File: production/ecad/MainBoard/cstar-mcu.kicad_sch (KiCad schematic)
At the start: 58 parts, among them J1 USB_C_Receptacle_USB2.0, J2 USB_C_Receptacle_USB2.0, J3 RX connect, J4 TX connect, J5 Ultra_1, J6 Ultra_2, J7 Ultra_3, J8 Ultra_4, Q1 AO3400A, Q2 AO3400A, Q3 AO3400A, Q4 AO3400A, SW1 SW_Push, SW2 SW_Push, SW3 SW_Push, SW4 SW_Push, U1 ESP32-WROOM-32UE_M113EH6400UH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, U2 CP2102N-A01-GQFN28, U3 TXB0104DR, U4 CP2102N-A01-GQFN28, U5 TXB0104DR, U6 ESP32-WROOM-32UE_M113EH6400UH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

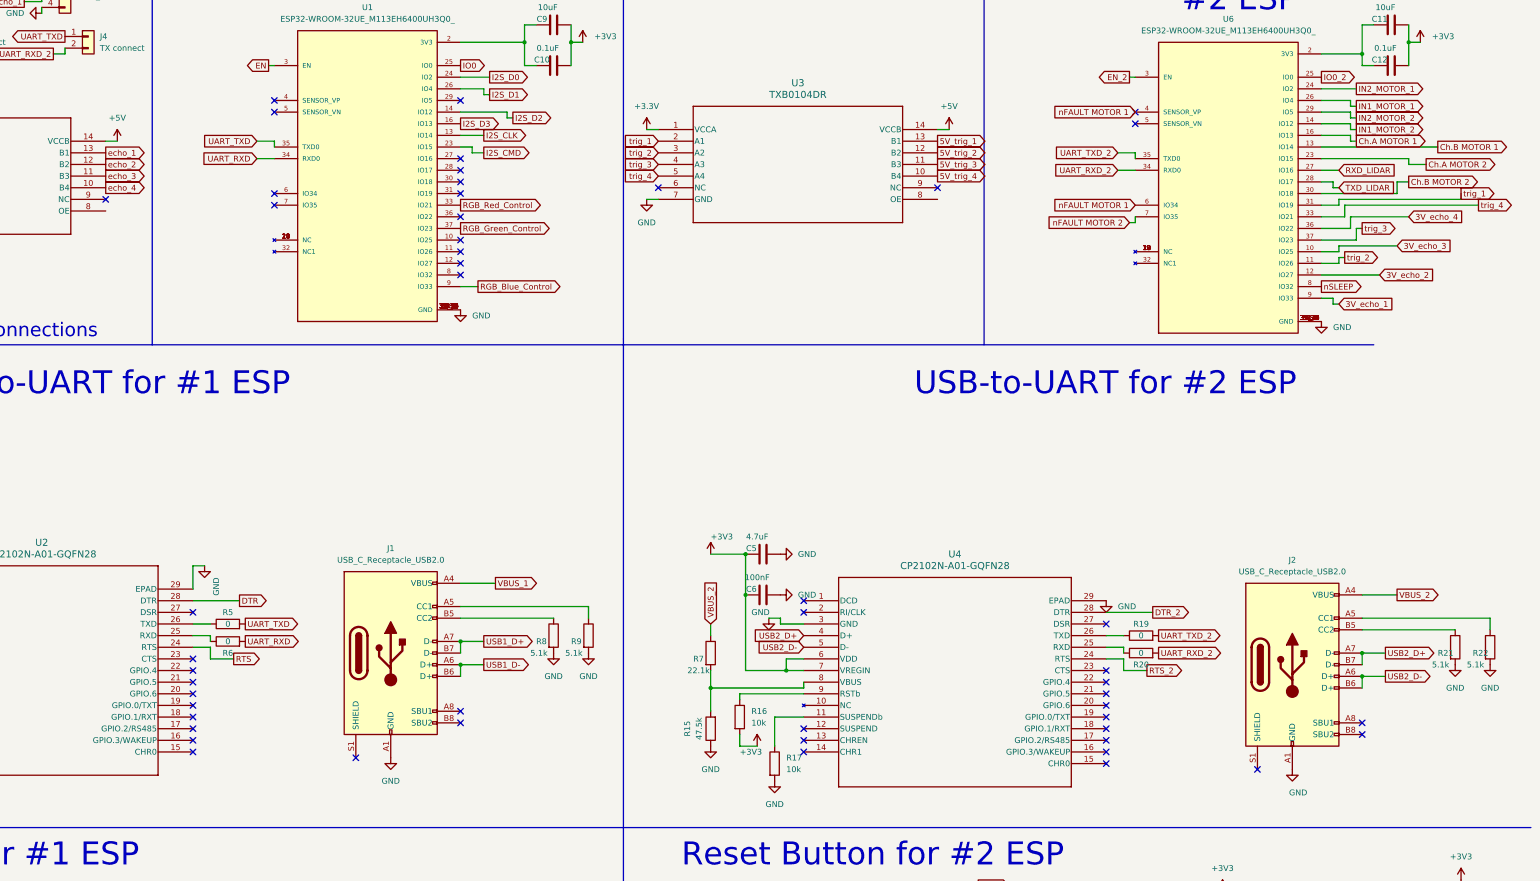
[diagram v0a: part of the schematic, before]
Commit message: Reversion of overcommited files
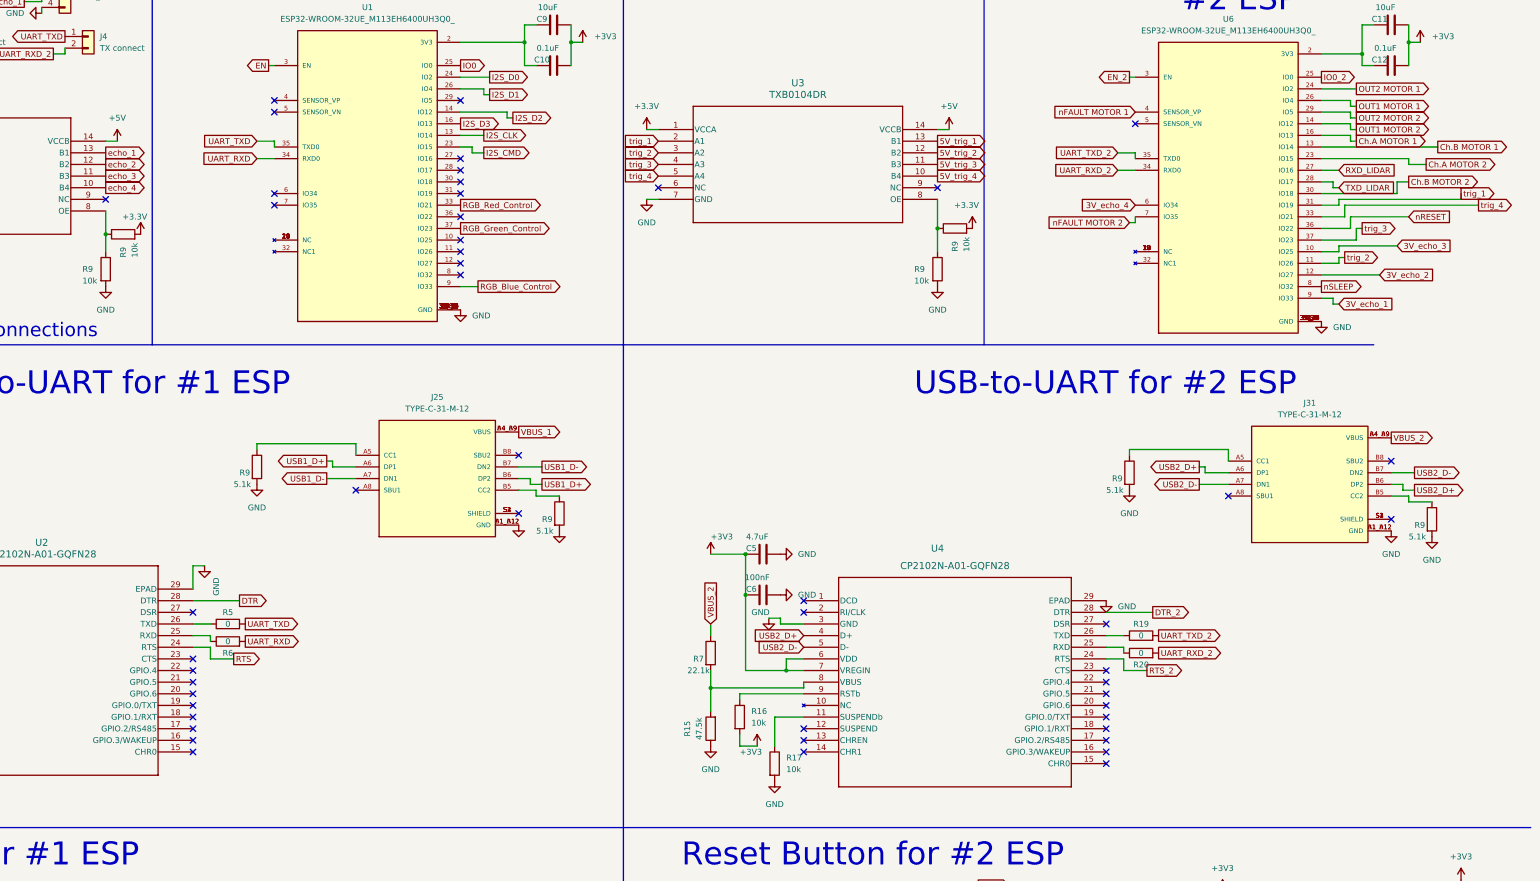
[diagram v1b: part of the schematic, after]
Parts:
- removed J1, J2: USB_C_Receptacle_USB2.0, CSTAR-MainBoard-Footprints:USBCONN-GCT_USB4105GFA, symbol Connector:USB_C_Receptacle_USB2.0
- removed R21, R22, R8, R9: 5.1k, Resistor_SMD:R_0805_2012Metric, symbol Device:R
- added J25, J31: TYPE-C-31-M-12, CSTAR-MainBoard-Footprints:HRO_TYPE-C-31-M-12, symbol TYPE-C-31-M-12:TYPE-C-31-M-12
- added R9 (x4): 10k, Resistor_SMD:R_0805_2012Metric, symbol Device:R
- added R9 (x4): 5.1k, Resistor_SMD:R_0805_2012Metric, symbol Device:R
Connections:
- net +3.3V: now also R9.2, R9.2
- net 3V_echo_4: now also U6.6 (IO34); no longer U6.36 (IO22)
- net GND: now also J25.A1_B12 (GND), J25.B1_A12 (GND), J31.A1_B12 (GND), J31.B1_A12 (GND), R9.2, R9.2, R9.2, R9.2, R9.2, R9.2
- net USB1_D+: now also J25.A6 (DP1), J25.B6 (DP2)
- net USB1_D-: now also J25.A7 (DN1), J25.B7 (DN2)
- net USB2_D+: now also J31.A6 (DP1), J31.B6 (DP2)
- net USB2_D-: now also J31.A7 (DN1), J31.B7 (DN2)
- net VBUS_1: now also J25.A4_B9 (VBUS), J25.B4_A9 (VBUS)
- net VBUS_2: now also J31.A4_B9 (VBUS), J31.B4_A9 (VBUS)
- net nFAULT MOTOR 1: no longer U6.6 (IO34)
- net at U5.8 (OE): now also R9.1, R9.1
- net at U3.8 (OE): now also R9.1, R9.1
- net IN1_MOTOR_1 renamed OUT1 MOTOR 1
- net IN1_MOTOR_2 renamed OUT1 MOTOR 2
- net IN2_MOTOR_1 renamed OUT2 MOTOR 1
- net IN2_MOTOR_2 renamed OUT2 MOTOR 2
- new net: J31.B5 (CC2), R9.1
- new net: J25.A5 (CC1), R9.1
- new net: J31.A5 (CC1), R9.1
- new net: J31.S1 (SHIELD), J31.S2 (SHIELD), J31.S3 (SHIELD), J31.S4 (SHIELD)
- new net: J25.B5 (CC2), R9.1
- new net: J25.S1 (SHIELD), J25.S2 (SHIELD), J25.S3 (SHIELD), J25.S4 (SHIELD)
- new net nRESET: U6.36 (IO22)
- no-connect marks 56 -> 55

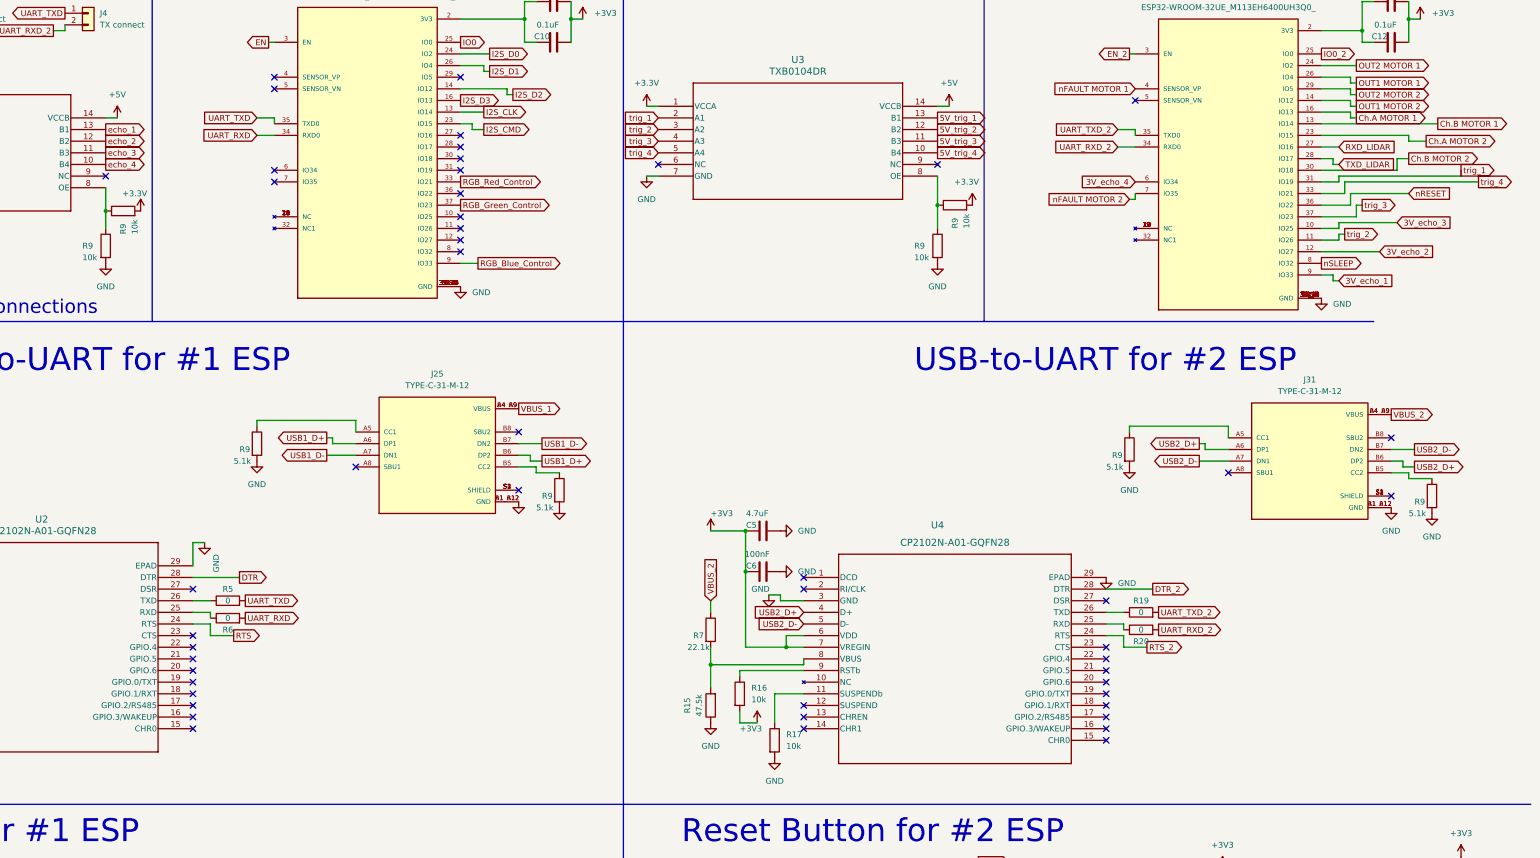
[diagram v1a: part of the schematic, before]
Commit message: "Added Backup Connector"
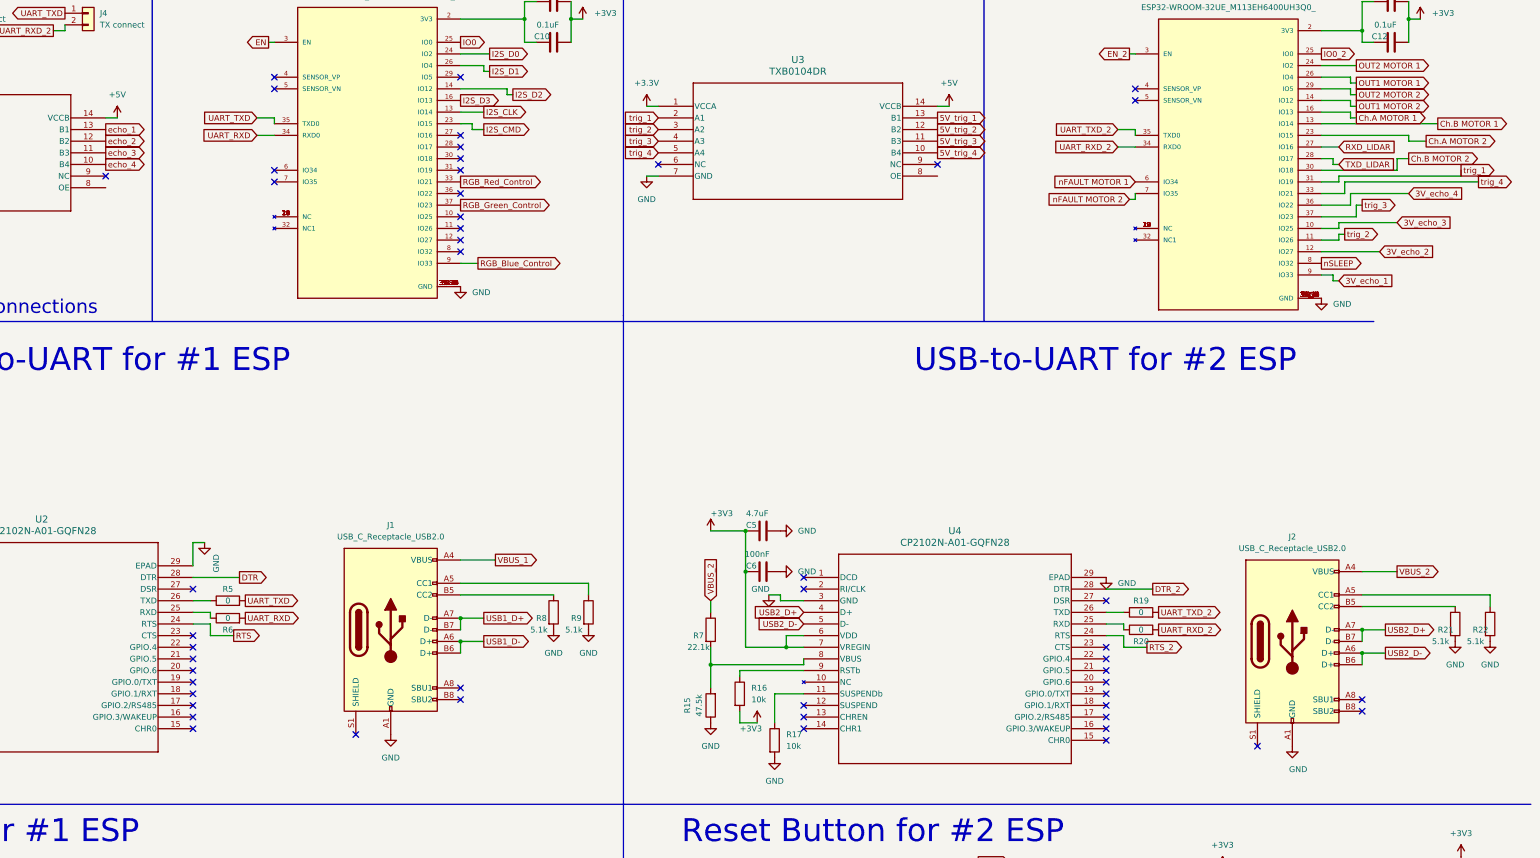
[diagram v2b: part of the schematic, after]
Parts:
- removed J25, J31: TYPE-C-31-M-12, CSTAR-MainBoard-Footprints:HRO_TYPE-C-31-M-12, symbol TYPE-C-31-M-12:TYPE-C-31-M-12
- removed R9 (x4): 10k, Resistor_SMD:R_0805_2012Metric, symbol Device:R
- removed R9 (x4): 5.1k, Resistor_SMD:R_0805_2012Metric, symbol Device:R
- added J1, J2: USB_C_Receptacle_USB2.0, CSTAR-MainBoard-Footprints:USBCONN-GCT_USB4105GFA, symbol Connector:USB_C_Receptacle_USB2.0
- added R21, R22, R8, R9: 5.1k, Resistor_SMD:R_0805_2012Metric, symbol Device:R
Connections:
- net nRESET is gone; now on net 3V_echo_4: U6.36 (IO22)
- net 3V_echo_4: no longer U6.6 (IO34)
- net GND: now also J1.A1 (GND), J1.A12 (GND), J1.B1 (GND), J1.B12 (GND), J2.A1 (GND), J2.A12 (GND), J2.B1 (GND), J2.B12 (GND), R21.2, R22.2, R8.2, R9.2
- net USB1_D+: now also J1.A7 (D-), J1.B7 (D-)
- net USB1_D-: now also J1.A6 (D+), J1.B6 (D+)
- net USB2_D+: now also J2.A7 (D-), J2.B7 (D-)
- net USB2_D-: now also J2.A6 (D+), J2.B6 (D+)
- net VBUS_1: now also J1.A4 (VBUS), J1.A9 (VBUS), J1.B4 (VBUS), J1.B9 (VBUS)
- net VBUS_2: now also J2.A4 (VBUS), J2.A9 (VBUS), J2.B4 (VBUS), J2.B9 (VBUS)
- net nFAULT MOTOR 1: now also U6.6 (IO34); no longer U6.4 (SENSOR_VP)
- new net: J2.A5 (CC1), R22.1
- new net: J1.A5 (CC1), R9.1
- new net: J2.B5 (CC2), R21.1
- new net: J1.B5 (CC2), R8.1
- no-connect marks 55 -> 56

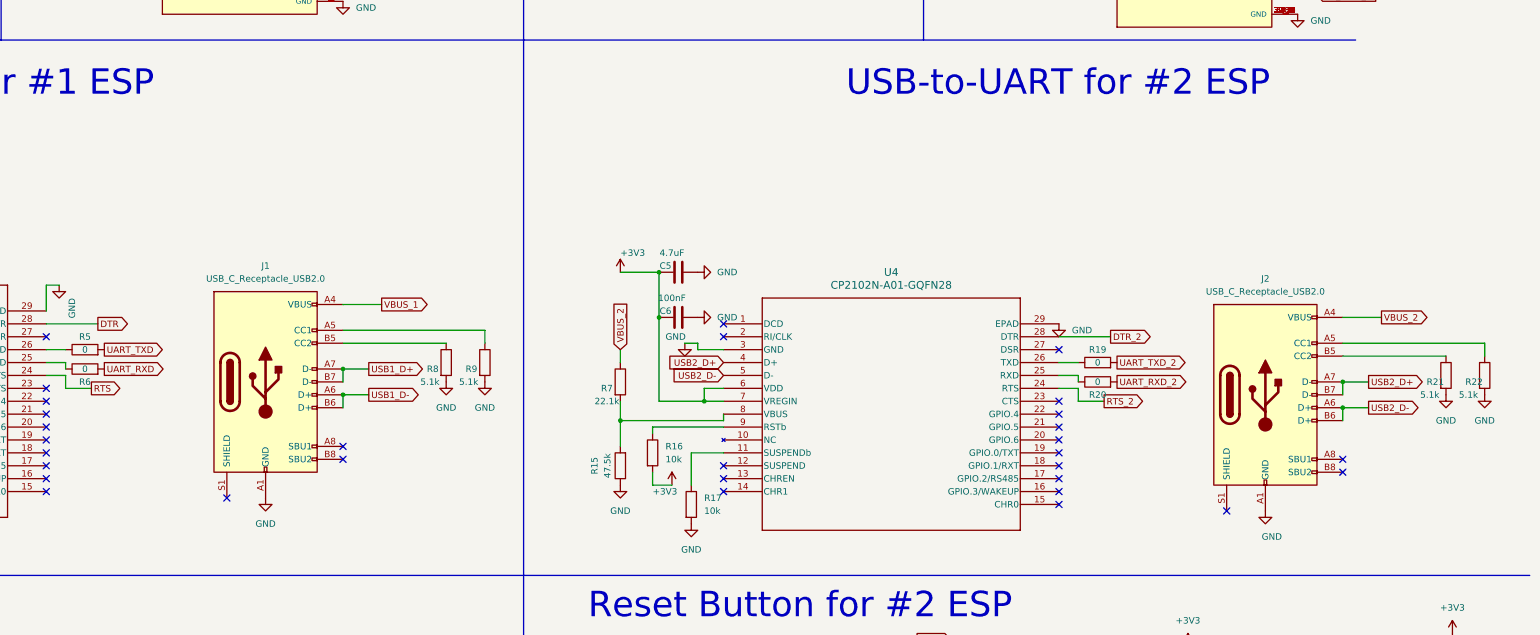
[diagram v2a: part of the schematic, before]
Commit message: fixed usbc connector
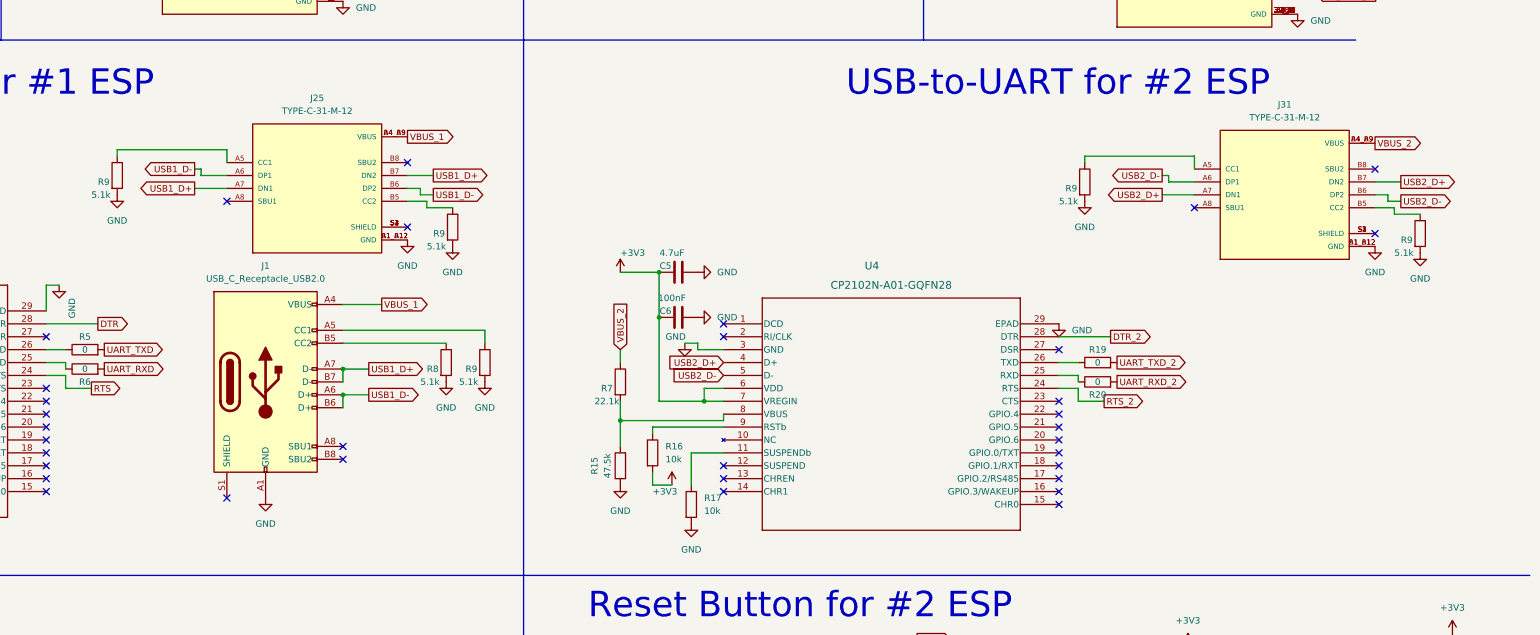
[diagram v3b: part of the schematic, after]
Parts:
- removed J2: USB_C_Receptacle_USB2.0, CSTAR-MainBoard-Footprints:USBCONN-GCT_USB4105GFA, symbol Connector:USB_C_Receptacle_USB2.0
- removed R21, R22: 5.1k, Resistor_SMD:R_0805_2012Metric, symbol Device:R
- added J25, J31: TYPE-C-31-M-12, TYPE-C-31-M-12:HRO_TYPE-C-31-M-12, symbol TYPE-C-31-M-12:TYPE-C-31-M-12
- added R9 (x4): 5.1k, Resistor_SMD:R_0805_2012Metric, symbol Device:R
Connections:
- net GND: now also J25.A1_B12 (GND), J25.B1_A12 (GND), J31.A1_B12 (GND), J31.B1_A12 (GND), R9.2, R9.2, R9.2, R9.2
- net USB1_D+: now also J25.A7 (DN1), J25.B7 (DN2)
- net USB1_D-: now also J25.A6 (DP1), J25.B6 (DP2)
- net USB2_D+: now also J31.A7 (DN1), J31.B7 (DN2)
- net USB2_D-: now also J31.A6 (DP1), J31.B6 (DP2)
- net VBUS_1: now also J25.A4_B9 (VBUS), J25.B4_A9 (VBUS)
- net VBUS_2: now also J31.A4_B9 (VBUS), J31.B4_A9 (VBUS)
- new net: J31.B5 (CC2), R9.1
- new net: J25.A5 (CC1), R9.1
- new net: J31.A5 (CC1), R9.1
- new net: J31.S1 (SHIELD), J31.S2 (SHIELD), J31.S3 (SHIELD), J31.S4 (SHIELD)
- new net: J25.B5 (CC2), R9.1
- new net: J25.S1 (SHIELD), J25.S2 (SHIELD), J25.S3 (SHIELD), J25.S4 (SHIELD)
- no-connect marks 56 -> 59
